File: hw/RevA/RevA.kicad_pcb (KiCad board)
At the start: 4 copper layers, 85 x 54 mm, 94 parts, among them J1 USB_C_Receptacle_USB2.0, J3 DNP Conn_01x02, J4 DNP Conn_02x03_Odd_Even, SW1 SW_Push, SW2 SW_Push, U1 SY8120B1ABC, U2 XC6206P25, U3 SY8120B1ABC, U4 SPI Flash W25Q128JVSIQ, U8 LFE5U-12F-6BG256C, U9 16MHz 20ppm

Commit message: progress
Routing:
- net +3V3: track 112.4 -> 62.4 mm, vias 43 -> 36
- net GND: track 151.4 -> 106.0 mm, vias 94 -> 89
- net /LED_B: track 37.0 -> 0.00 mm, vias 2 -> 0
- net /LED_G: track 35.9 -> 0.00 mm, vias 2 -> 0
- net /LED_R: track 35.0 -> 0.00 mm, vias 2 -> 0
- net /JTAG_TDO: track 57.9 -> 35.2 mm, vias 3 -> 2
- net Net-(U8-PadR1): track 21.9 -> 0.00 mm
- net Net-(U8-PadB11): track 21.7 -> 0.00 mm
- net /FPGA_DONE: track 21.4 -> 0.00 mm
- net Net-(U8-PadB12): track 19.9 -> 0.00 mm
- net Net-(U8-PadA12): track 19.8 -> 0.00 mm
- net Net-(U8-PadT2): track 18.9 -> 0.00 mm
- net /FPGA_~INIT: track 18.6 -> 0.00 mm, vias 2 -> 0
- net Net-(U8-PadA13): track 18.0 -> 0.00 mm
- net Net-(U8-PadC6): track 17.8 -> 0.02 mm, vias 2 -> 0
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
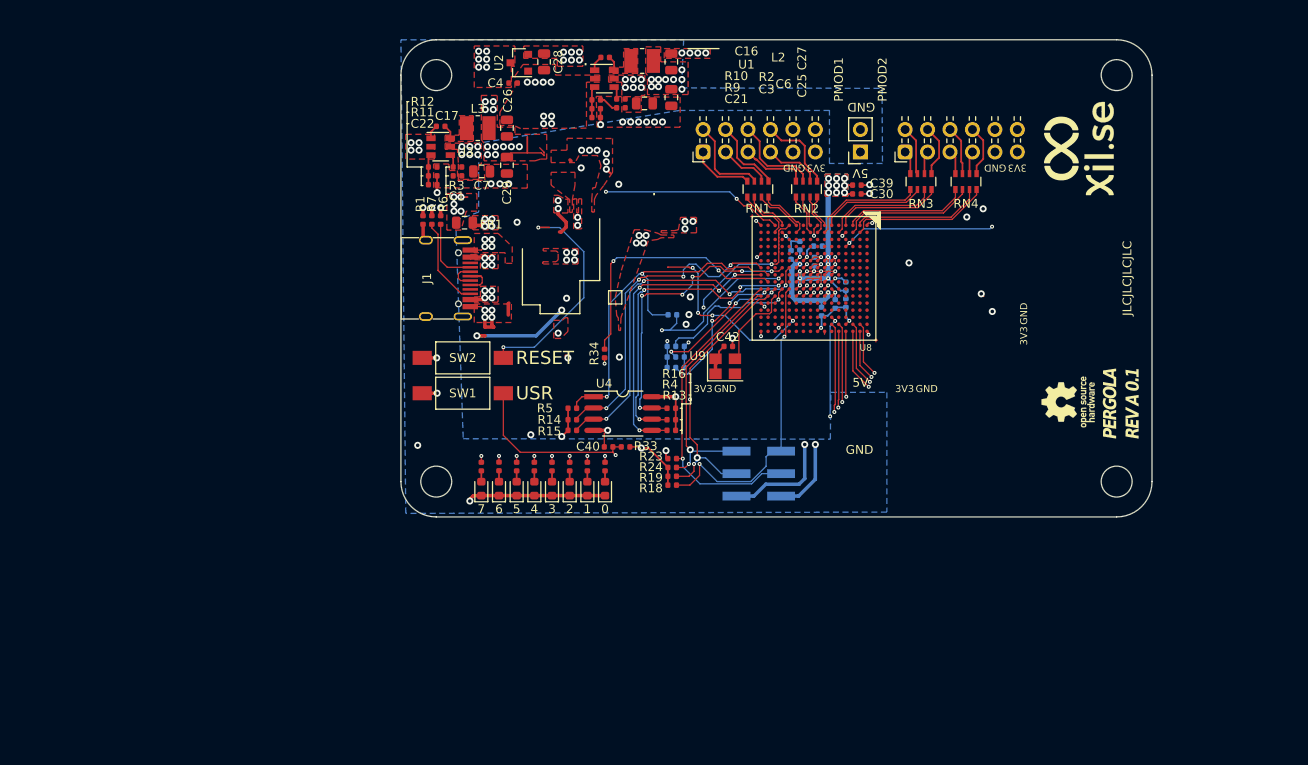
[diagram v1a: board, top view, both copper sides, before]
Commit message: Import pcb shape
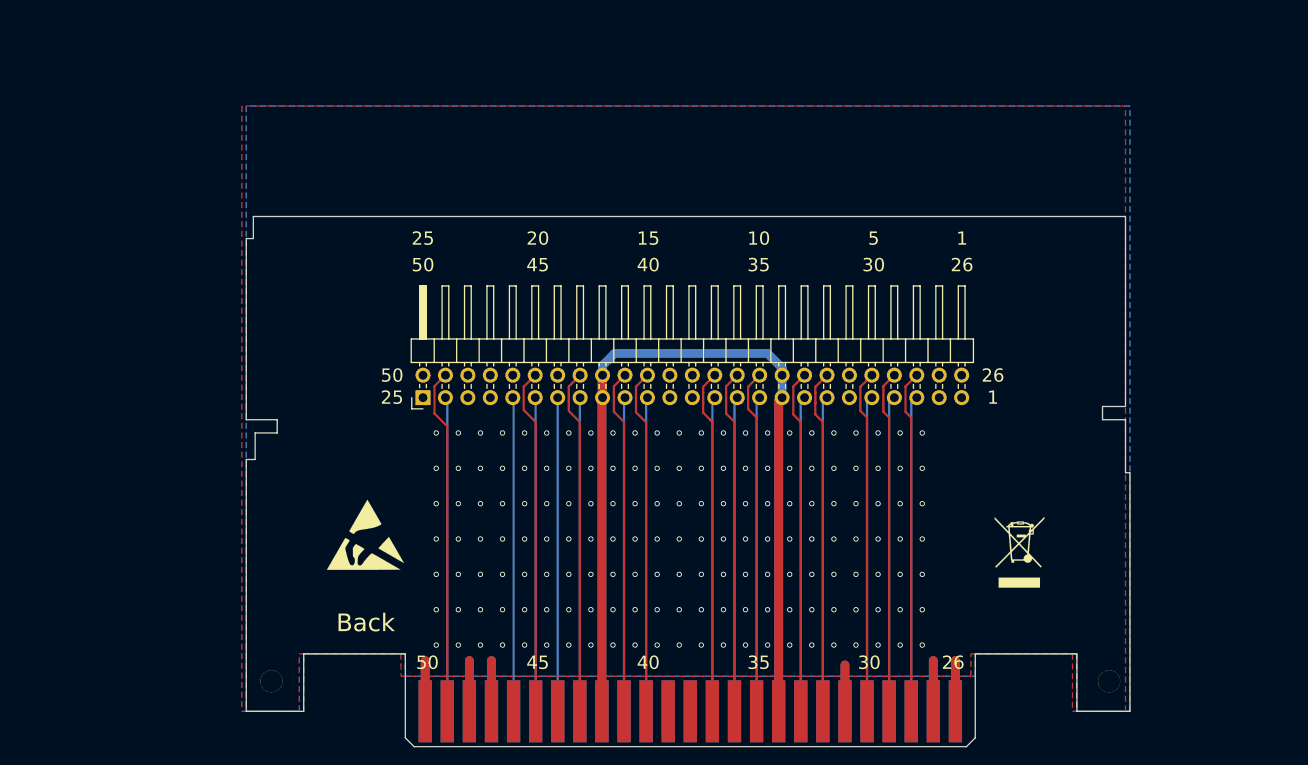
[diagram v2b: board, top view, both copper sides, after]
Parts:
- removed C1, C16, C17, C3, C30, C31, C32, C33, C34, C35, C36, C37, C38, C39, C40, C42: 100n, Capacitor_SMD:C_0402_1005Metric
- removed C21, C22: 22p, Capacitor_SMD:C_0402_1005Metric
- removed C25, C26, C27, C28, C29, C6, C7: 22u, Capacitor_SMD:C_0805_2012Metric
- removed C4: 4u7, Capacitor_SMD:C_0402_1005Metric
- removed D2, D3, D4, D5, D6, D7, D8, D9: LED, LED_SMD:LED_0603_1608Metric
- removed FB1: Ferrite_Bead, Inductor_SMD:L_0805_2012Metric
- removed H1, H2, H3, H4: DNP, MountingHole:MountingHole_3.5mm
- removed J3: DNP Conn_01x02, Connector_PinSocket_2.54mm:PinSocket_1x02_P2.54mm_Vertical
- removed J4: DNP Conn_02x03_Odd_Even, Connector_PinHeader_2.54mm:PinHeader_2x03_P2.54mm_Vertical_SMD
- removed JP7, JP8, JP9: 4K7, ecp5board:JP_3_0402_1005Metric
- removed L2, L3: 4u7 1A, ecp5board:L_1008_1210
- removed LOGO1: Logo_Open_Hardware_Small, Symbol:OSHW-Logo_5.7x6mm_SilkScreen
- removed LOGO2: Logo_Open_Hardware_Small, ecp5board:logo
- removed LOGO3: Logo_Open_Hardware_Small, ecp5board:xil_logo_new
- removed PMOD1, PMOD2: Conn_02x06_Top_Bottom, ecp5board:PMOD_Socket_2x06_P2.54mm_Horizontal
- removed R1: 100K, Resistor_SMD:R_0402_1005Metric
- removed R10: 18K, Resistor_SMD:R_0402_1005Metric
- removed R11, R9: 15K, Resistor_SMD:R_0402_1005Metric
- removed R12: 3K3, Resistor_SMD:R_0402_1005Metric
- removed R13, R14, R15, R16, R2, R25, R26, R27, R28, R29, R3, R30, R31, R32: 10K, Resistor_SMD:R_0402_1005Metric
- removed R18, R19, R23, R24, R33, R34, R5: 4K7, Resistor_SMD:R_0402_1005Metric
- removed R35: DNP, Resistor_SMD:R_0402_1005Metric
- removed R4: 1K, Resistor_SMD:R_0402_1005Metric
- removed R6, R7: 5K1, Resistor_SMD:R_0402_1005Metric
- removed RN1, RN2, RN3, RN4: 22R_x4, Resistor_SMD:R_Array_Convex_4x0603
- removed SW1, SW2: SW_Push, Button_Switch_SMD:SW_SPST_FSMSM
- removed U1, U3: SY8120B1ABC, Package_TO_SOT_SMD:SOT-23-6
- removed U2: XC6206P25, Package_TO_SOT_SMD:SOT-23
- removed U4: SPI Flash W25Q128JVSIQ, ecp5board:SOA008-150-208mil
- removed U8: LFE5U-12F-6BG256C, w_smd_bga:cabga256
- removed U9: 16MHz 20ppm, Crystal:Crystal_SMD_3225-4Pin_3.2x2.5mm
- added CON1: N64-Cartridge, Brutzelkarte:N64-Connector, B.Cu at (132.8, 126.0)
- added REF**: ESD-Logo_8.9x8mm_SilkScreen, Symbol:ESD-Logo_8.9x8mm_SilkScreen, F.Cu at (96.0, 106.0)
- added REF**: WEEE-Logo_5.6x8mm_SilkScreen, Symbol:WEEE-Logo_5.6x8mm_SilkScreen, F.Cu at (170.0, 108.0)
- added REF**: MountingHole_2.5mm_Pad, MountingHole:MountingHole_2.5mm_Pad, F.Cu at (180.2, 122.6)
- added REF**: MountingHole_2.5mm_Pad, MountingHole:MountingHole_2.5mm_Pad, F.Cu at (85.3, 122.6)
- J1: value USB_C_Receptacle_USB2.0 -> Conn_02x25_Odd_Even; footprint Connector_USB_Extra:USB_C_Receptacle_GT-USB-7010 -> Connector_PinHeader_2.54mm:PinHeader_2x25_P2.54mm_Horizontal
- moved J1 13.7 mm to (102.5, 90.5), turned to 90 degrees
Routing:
- net /fpga/N64_VCC: track 0.00 -> 173.5 mm
- net /LED7: track 63.4 -> 0.00 mm, vias 2 -> 0
- net +3V3: track 62.4 -> 0.00 mm, vias 36 -> 0
- net /SW_USER: track 62.0 -> 0.00 mm, vias 3 -> 0
- net /LED6: track 60.0 -> 0.00 mm, vias 2 -> 0
- net /LED5: track 58.5 -> 0.00 mm, vias 2 -> 0
- net /LED4: track 55.1 -> 0.00 mm, vias 2 -> 0
- net /LED3: track 50.4 -> 0.00 mm, vias 2 -> 0
- net /LED2: track 48.8 -> 0.00 mm, vias 2 -> 0
- net /LED1: track 45.3 -> 0.00 mm, vias 2 -> 0
- net /LED0: track 43.6 -> 0.00 mm, vias 2 -> 0
- net /FPGA_SPI_~CS~: track 42.5 -> 0.00 mm, vias 2 -> 0
- net /FPGA_SPI_D2: track 40.9 -> 0.00 mm, vias 4 -> 0
- net /fpga/N64_AD5: track 0.00 -> 39.4 mm
- net /fpga/N64_RAUDIO: track 0.00 -> 39.2 mm
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- added copper zone on B.Cu, net GND
- removed copper zone on B.Cu, net +1V1
- removed copper zone on F.Cu, net +1V1
- removed copper zone on In2.Cu, net +1V1
- removed copper zone on F.Cu, net +2V5
- removed copper zone on In2.Cu, net +2V5
- removed copper zone on F.Cu, net +3V3
- removed copper zone on In2.Cu, net +3V3
- removed copper zone on F.Cu, net /DCDC_OUT
- removed copper zone on In2.Cu, net /DCDC_OUT
- removed copper zone on In1.Cu, net /USB_SHIELD
- removed copper zone on F.Cu, net /VBUS_UNFILTERED
- removed copper zone on In2.Cu, net /VBUS_UNFILTERED
- removed copper zone on In1.Cu, net GND
- removed copper zone on In2.Cu, net GND
- removed copper zone on F.Cu, net Net-(C16-Pad2)
- removed copper zone on F.Cu, net Net-(C17-Pad2)
- removed copper zone on F.Cu, net Net-(L1-Pad2)
- removed copper zone on B.Cu, net VBUS
- removed copper zone on F.Cu, net VBUS
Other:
- board size 85 x 54 mm -> 100 x 60 mm
- copper layers 4 -> 2
- net class Default: clearance 0.127 -> 0.25; trace_width 0.127 -> 0.25; via_dia 0.45 -> 0.6; via_drill 0.2 -> 0.4
- net class differential routing added: clearance 0.4, trace_width 0.25, via_dia 0.6, via_drill 0.4
- rule pad_to_mask_clearance: 0.051 -> 0.13
- rule solder_mask_min_width: 0.25 -> 0.3
- rule trace_clearance: 0.127 -> 0.25
- rule trace_min: 0.0889 -> 0.1
- rule via_min_drill: 0.2 -> 0.3
- rule via_min_size: 0.45 -> 0.5
- board text added: "10"
- board text added: "15"
- board text added: "20"
- board text added: "25"
- board text added: "26"
- board text added: "30"
- board text added: "35"
- board text added: "40"
- board text added: "45"
- board text added: "50"
- board text removed: "."
- board text removed: "0"
- board text removed: "2"
- board text removed: "3"
- board text removed: "3V3"
- board text removed: "4"
- board text removed: "5V"
- board text removed: "6"
- board text removed: "7"
- board text removed: "Designed by @kbeckmann"
- board text removed: "ECP5_CFG_0"
- board text removed: "ECP5_CFG_1"
- board text removed: "ECP5_CFG_2"
- board text removed: "GND"
- board text removed: "IMX_BOOT_MODE_0"
- board text removed: "IMX_BOOT_MODE_1"
- board text removed: "IMX_CFG_0"
- board text removed: "IMX_CFG_1"
- board text removed: "IMX_CFG_2"
- board text removed: "IMX_CFG_3"
- board text removed: "JLCJLCJLCJLC"
- board text removed: "PMOD1"
- board text removed: "PMOD2"
- board text removed: "PMOD3"
- board text removed: "PMOD4"
- board text removed: "PMOD5"
- board text removed: "Place 0R to connect ECP5_MASTER_SPI_CSN to FLASH_CSN"
- board text removed: "RESET"
- board text removed: "SWCLK"
- board text removed: "SWDIO"
- board text removed: "TCK"
- board text removed: "TDI"
- board text removed: "TDO"
- board text removed: "TMS"
- board text removed: "USR"
- board text removed: "VCC"
- board text removed: "https://pergola.xil.se"

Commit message: progress
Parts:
- removed the REF** at (96.0, 106.0)
- removed the REF** at (170.0, 108.0)
- removed the REF** at (180.2, 122.6)
- removed the REF** at (85.3, 122.6)
- added C1: 100n, Capacitor_SMD:C_0402_1005Metric, F.Cu at (73.5, 85.0)
- added C16: 100n, Capacitor_SMD:C_0402_1005Metric, F.Cu at (87.1, 92.1)
- added C17: 100n, Capacitor_SMD:C_0402_1005Metric, F.Cu at (76.4, 82.9)
- added C2: 100n, Capacitor_SMD:C_0402_1005Metric, F.Cu at (87.9, 70.9)
- added C21: 22p, Capacitor_SMD:C_0402_1005Metric, F.Cu at (73.2, 100.7)
- added C22: 22p, Capacitor_SMD:C_0402_1005Metric, F.Cu at (80.3, 93.7)
- added C25: 22u, Capacitor_SMD:C_0805_2012Metric, F.Cu at (62.5, 72.3)
- added C26: 22u, Capacitor_SMD:C_0805_2012Metric, F.Cu at (67.0, 72.2)
- added C27: 22u, Capacitor_SMD:C_0805_2012Metric, F.Cu at (68.3, 91.1)
- added C28: 22u, Capacitor_SMD:C_0805_2012Metric, F.Cu at (75.5, 71.9)
- added C29: 22u, Capacitor_SMD:C_0805_2012Metric, F.Cu at (64.0, 83.6)
- added C3: 100n, Capacitor_SMD:C_0402_1005Metric, F.Cu at (87.9, 68.9)
- added C30: 100n, Capacitor_SMD:C_0402_1005Metric, F.Cu at (82.8, 75.7)
- added C31: 100n, Capacitor_SMD:C_0402_1005Metric, F.Cu at (76.0, 81.0)
- added C32: 100n, Capacitor_SMD:C_0402_1005Metric, F.Cu at (87.1, 90.1)
- added C33: 100n, Capacitor_SMD:C_0402_1005Metric, F.Cu at (77.4, 94.8)
- added C34: 100n, Capacitor_SMD:C_0402_1005Metric, F.Cu at (85.0, 72.1)
- added C35: 100n, Capacitor_SMD:C_0402_1005Metric, F.Cu at (79.9, 77.7)
- added C36: 100n, Capacitor_SMD:C_0402_1005Metric, F.Cu at (73.2, 98.7)
- added C37: 100n, Capacitor_SMD:C_0402_1005Metric, F.Cu at (79.9, 75.7)
- added C38: 100n, Capacitor_SMD:C_0402_1005Metric, F.Cu at (73.5, 83.0)
- added C39: 100n, Capacitor_SMD:C_0402_1005Metric, F.Cu at (81.5, 89.8)
- added C4: 4u7, Capacitor_SMD:C_0402_1005Metric, F.Cu at (80.3, 91.8)
- added C40: 100n, Capacitor_SMD:C_0402_1005Metric, F.Cu at (70.3, 100.7)
- added C42: 100n, Capacitor_SMD:C_0402_1005Metric, F.Cu at (74.5, 96.8)
- added C5: 100n, Capacitor_SMD:C_0402_1005Metric, F.Cu at (78.9, 81.0)
- added C6: 22u, Capacitor_SMD:C_0805_2012Metric, F.Cu at (79.7, 67.3)
- added C7: 22u, Capacitor_SMD:C_0805_2012Metric, F.Cu at (58.1, 72.3)
- added D2: LED, LED_SMD:LED_0603_1608Metric, F.Cu at (75.0, 74.7)
- added D3: LED, LED_SMD:LED_0603_1608Metric, F.Cu at (84.3, 65.8)
- added D4: LED, LED_SMD:LED_0603_1608Metric, F.Cu at (68.1, 96.5)
- added D5: LED, LED_SMD:LED_0603_1608Metric, F.Cu at (64.0, 100.6)
- added D6: LED, LED_SMD:LED_0603_1608Metric, F.Cu at (84.3, 63.2)
- added D7: LED, LED_SMD:LED_0603_1608Metric, F.Cu at (64.0, 98.0)
- added D8: LED, LED_SMD:LED_0603_1608Metric, F.Cu at (68.1, 93.9)
- added D9: LED, LED_SMD:LED_0603_1608Metric, F.Cu at (60.0, 60.9)
- added DBG1: Conn_02x06_Top_Bottom, ecp5board:PMOD_Socket_2x06_P2.54mm_Horizontal, F.Cu at (125.9, 60.2)
- added FB1: Ferrite_Bead, Inductor_SMD:L_0805_2012Metric, F.Cu at (70.1, 60.4)
- added J2: Micro_SD_Card, Connector_Card:microSD_HC_Molex_104031-0811, F.Cu at (191.5, 67.0)
- added J3: DNP Conn_01x02, Connector_PinSocket_2.54mm:PinSocket_1x02_P2.54mm_Vertical, F.Cu at (160.2, 66.2)
- added JP1: 4K7, Connector_PinHeader_2.54mm:PinHeader_1x03_P2.54mm_Horizontal, F.Cu at (106.0, 92.5)
- added JP7: 4K7, ecp5board:JP_3_0402_1005Metric, F.Cu at (74.8, 88.8)
- added JP8: 4K7, ecp5board:JP_3_0402_1005Metric, F.Cu at (65.5, 81.0)
- added JP9: 4K7, ecp5board:JP_3_0402_1005Metric, F.Cu at (73.9, 60.0)
- added L2: 4u7 1A, ecp5board:L_1008_1210, F.Cu at (76.4, 108.6)
- added L3: 4u7 1A, ecp5board:L_1008_1210, F.Cu at (82.0, 108.6)
- added LOGO1: Logo_Open_Hardware_Small, Symbol:OSHW-Logo_5.7x6mm_SilkScreen, F.Cu at (189.8, 105.5)
- added LOGO3: Logo_Open_Hardware_Small, ecp5board:xil_logo_new, F.Cu at (112.0, 105.5)
- added PMOD1: Conn_02x06_Top_Bottom, ecp5board:PMOD_Socket_2x06_P2.54mm_Horizontal, F.Cu at (148.7, 60.2)
- added PMOD2: Conn_02x06_Top_Bottom, ecp5board:PMOD_Socket_2x06_P2.54mm_Horizontal, F.Cu at (171.6, 60.2)
- added R1: 100K, Resistor_SMD:R_0402_1005Metric, F.Cu at (77.4, 92.8)
- added R10: 18K, Resistor_SMD:R_0402_1005Metric, F.Cu at (88.0, 84.2)
- added R11: 15K, Resistor_SMD:R_0402_1005Metric, F.Cu at (72.0, 90.8)
- added R12: 3K3, Resistor_SMD:R_0402_1005Metric, F.Cu at (74.9, 90.8)
- added R13: 10K, Resistor_SMD:R_0402_1005Metric, F.Cu at (74.1, 77.0)
- added R14: 10K, Resistor_SMD:R_0402_1005Metric, F.Cu at (67.5, 98.7)
- added R15: 10K, Resistor_SMD:R_0402_1005Metric, F.Cu at (77.0, 79.0)
- added R16: 10K, Resistor_SMD:R_0402_1005Metric, F.Cu at (88.0, 80.2)
- added R17: 22R, Resistor_SMD:R_0402_1005Metric, F.Cu at (88.0, 86.2)
- added R18: 4K7, Resistor_SMD:R_0402_1005Metric, F.Cu at (79.2, 73.7)
- added R19: 4K7, Resistor_SMD:R_0402_1005Metric, F.Cu at (87.8, 64.9)
- added R2: 10K, Resistor_SMD:R_0402_1005Metric, F.Cu at (87.9, 66.9)
- added R20: 1K, Resistor_SMD:R_0402_1005Metric, F.Cu at (71.6, 95.5)
- added R21: 4K7, Resistor_SMD:R_0402_1005Metric, F.Cu at (67.7, 85.0)
- added R22: 10K, Resistor_SMD:R_0402_1005Metric, F.Cu at (73.2, 81.0)
- added R23: 4K7, Resistor_SMD:R_0402_1005Metric, F.Cu at (67.5, 100.7)
- added R24: 4K7, Resistor_SMD:R_0402_1005Metric, F.Cu at (77.0, 77.0)
- added R25: 10K, Resistor_SMD:R_0402_1005Metric, F.Cu at (82.1, 71.8)
- added R26: 10K, Resistor_SMD:R_0402_1005Metric, F.Cu at (70.6, 83.0)
- added R27: 10K, Resistor_SMD:R_0402_1005Metric, F.Cu at (85.0, 68.1)
- added R28: 10K, Resistor_SMD:R_0402_1005Metric, F.Cu at (78.6, 89.8)
- added R29: 10K, Resistor_SMD:R_0402_1005Metric, F.Cu at (70.4, 98.7)
- added R3: 10K, Resistor_SMD:R_0402_1005Metric, F.Cu at (88.0, 82.2)
- added R30: 10K, Resistor_SMD:R_0402_1005Metric, F.Cu at (74.1, 79.0)
- added R31: 10K, Resistor_SMD:R_0402_1005Metric, F.Cu at (88.0, 78.2)
- added R32: 10K, Resistor_SMD:R_0402_1005Metric, F.Cu at (74.5, 92.8)
- added R33: 4K7, Resistor_SMD:R_0402_1005Metric, F.Cu at (74.5, 94.8)
- added R34: 4K7, Resistor_SMD:R_0402_1005Metric, F.Cu at (85.0, 70.1)
- added R35: 10K, Resistor_SMD:R_0402_1005Metric, F.Cu at (70.6, 85.0)
- added R36: 10K, Resistor_SMD:R_0402_1005Metric, F.Cu at (82.1, 73.7)
- added R37: 10K, Resistor_SMD:R_0402_1005Metric, F.Cu at (87.0, 88.2)
- added R4: 1K, Resistor_SMD:R_0402_1005Metric, F.Cu at (79.2, 69.8)
- added R5: 4K7, Resistor_SMD:R_0402_1005Metric, F.Cu at (67.7, 83.0)
- added R6: 5K1, Resistor_SMD:R_0402_1005Metric, F.Cu at (71.6, 93.6)
- added R7: 5K1, Resistor_SMD:R_0402_1005Metric, F.Cu at (87.8, 63.0)
- added R8: 22R, Resistor_SMD:R_0402_1005Metric, F.Cu at (82.1, 69.8)
- added R9: 15K, Resistor_SMD:R_0402_1005Metric, F.Cu at (79.2, 71.8)
- added REF**: MountingHole_2.5mm_Pad, MountingHole:MountingHole_2.5mm_Pad, F.Cu at (197.7, 112.6)
- added REF**: MountingHole_2.5mm_Pad, MountingHole:MountingHole_2.5mm_Pad, F.Cu at (102.8, 112.6)
- added RN1: 22R_x4, Resistor_SMD:R_Array_Convex_4x0603, F.Cu at (144.0, 77.0)
- added RN10: 22R_x4, Resistor_SMD:R_Array_Convex_4x0603, F.Cu at (149.5, 106.0)
- added RN11: 22R_x4, Resistor_SMD:R_Array_Convex_4x0603, F.Cu at (140.5, 106.0)
- added RN12: 22R_x4, Resistor_SMD:R_Array_Convex_4x0603, F.Cu at (131.5, 106.0)
- added RN2: 22R_x4, Resistor_SMD:R_Array_Convex_4x0603, F.Cu at (149.5, 77.0)
- added RN3: 22R_x4, Resistor_SMD:R_Array_Convex_4x0603, F.Cu at (167.0, 77.0)
- added RN4: 22R_x4, Resistor_SMD:R_Array_Convex_4x0603, F.Cu at (172.5, 77.0)
- added RN5: 22R_x4, Resistor_SMD:R_Array_Convex_4x0603, F.Cu at (158.5, 106.0)
- added RN6: 22R_x4, Resistor_SMD:R_Array_Convex_4x0603, F.Cu at (154.0, 106.0)
- added RN7: 22R_x4, Resistor_SMD:R_Array_Convex_4x0603, F.Cu at (145.0, 106.0)
- added RN8: 22R_x4, Resistor_SMD:R_Array_Convex_4x0603, F.Cu at (136.0, 106.0)
- added RN9: 22R_x4, Resistor_SMD:R_Array_Convex_4x0603, F.Cu at (163.0, 106.0)
- added SW1: SW_Push, Button_Switch_SMD:SW_SPST_FSMSM, F.Cu at (192.0, 77.0)
- added U1: SY8120B1ABC, Package_TO_SOT_SMD:SOT-23-6, F.Cu at (75.7, 63.3)
- added U2: XC6206P25, Package_TO_SOT_SMD:SOT-23, F.Cu at (70.4, 77.8)
- added U3: SY8120B1ABC, Package_TO_SOT_SMD:SOT-23-6, F.Cu at (80.8, 101.2)
- added U4: SPI Flash W25Q128JVSIQ, ecp5board:SOA008-150-208mil, F.Cu at (129.2, 86.2)
- added U6: IS42S16320F-7TL, Package_SO:TSOP-II-54_22.2x10.16mm_P0.8mm, F.Cu at (176.5, 90.0)
- added U7: SPI Flash W25Q128JVSIQ, ecp5board:SOA008-150-208mil, F.Cu at (129.5, 93.2)
- added U8: LFE5U-12F-6BG256C, w_smd_bga:cabga256, F.Cu at (150.0, 90.0)
- added U9: 16MHz 20ppm, Crystal:Crystal_SMD_3225-4Pin_3.2x2.5mm, F.Cu at (160.0, 77.0)
- CON1: footprint Brutzelkarte:N64-Connector -> ecp5board:N64-Connector
- J1: value Conn_02x25_Odd_Even -> USB_C_Receptacle_USB2.0; footprint Connector_PinHeader_2.54mm:PinHeader_2x25_P2.54mm_Horizontal -> Connector_USB_Extra:USB_C_Receptacle_GT-USB-7010
- moved J1 23.2 mm to (105.2, 67.5), turned to 270 degrees
- moved CON1 20.2 mm to (150.2, 116.0)
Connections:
- CON1 pad 10: /fpga/N64_READ -> /N64_READ
- CON1 pad 11: /fpga/N64_AD11 -> /N64_AD11
- CON1 pad 12: /fpga/N64_AD10 -> /N64_AD10
- CON1 pad 15: /fpga/N64_AD9 -> /N64_AD9
- CON1 pad 16: /fpga/N64_AD8 -> /N64_AD8
- CON1 pad 17: /fpga/N64_VCC -> /N64_VCC
- CON1 pad 18: /fpga/N64_CIC_DIO -> /N64_CIC_DIO
- CON1 pad 19: /fpga/N64_SI_CLK -> /N64_SI_CLK
- CON1 pad 20: /fpga/N64_CR -> /N64_CR
- CON1 pad 21: /fpga/N64_EEP_SDAT -> /N64_EEP_SDAT
- CON1 pad 24: /fpga/N64_LAUDIO -> /N64_LAUDIO
- CON1 pad 28: /fpga/N64_AD0 -> /N64_AD0
- CON1 pad 29: /fpga/N64_AD1 -> /N64_AD1
- CON1 pad 3: /fpga/N64_AD15 -> /N64_AD15
- CON1 pad 30: /fpga/N64_AD2 -> /N64_AD2
- CON1 pad 32: /fpga/N64_AD3 -> /N64_AD3
- CON1 pad 33: /fpga/N64_ALEL -> /N64_ALEL
- CON1 pad 34: /fpga/N64_VCC -> /N64_VCC
- CON1 pad 35: /fpga/N64_ALEH -> /N64_ALEH
- CON1 pad 36: /fpga/N64_AD4 -> /N64_AD4
- CON1 pad 37: /fpga/N64_AD5 -> /N64_AD5
- CON1 pad 4: /fpga/N64_AD14 -> /N64_AD14
- CON1 pad 40: /fpga/N64_AD6 -> /N64_AD6
- CON1 pad 41: /fpga/N64_AD7 -> /N64_AD7
- CON1 pad 42: /fpga/N64_VCC -> /N64_VCC
- CON1 pad 43: /fpga/N64_CIC_DCLK -> /N64_CIC_DCLK
- CON1 pad 45: /fpga/N64_NMI -> /N64_NMI
- CON1 pad 49: /fpga/N64_RAUDIO -> /N64_RAUDIO
- CON1 pad 5: /fpga/N64_AD13 -> /N64_AD13
- CON1 pad 7: /fpga/N64_AD12 -> /N64_AD12
- CON1 pad 8: /fpga/N64_WRITE -> /N64_WRITE
- CON1 pad 9: /fpga/N64_VCC -> /N64_VCC
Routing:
- net /fpga/N64_VCC: track 173.5 -> 0.00 mm
- net /fpga/N64_AD5: track 39.4 -> 0.00 mm
- net /fpga/N64_RAUDIO: track 39.2 -> 0.00 mm
- net /fpga/N64_NMI: track 39.1 -> 0.00 mm
- net /fpga/N64_CIC_DCLK: track 39.1 -> 0.00 mm
- net /fpga/N64_AD6: track 39.1 -> 0.00 mm
- net /fpga/N64_AD7: track 39.0 -> 0.00 mm
- net /fpga/N64_ALEH: track 39.0 -> 0.00 mm
- net /fpga/N64_AD4: track 39.0 -> 0.00 mm
- net /fpga/N64_AD3: track 38.9 -> 0.00 mm
- net /fpga/N64_ALEL: track 38.9 -> 0.00 mm
- net /fpga/N64_AD2: track 38.9 -> 0.00 mm
- net /fpga/N64_AD0: track 38.8 -> 0.00 mm
- net /fpga/N64_AD1: track 38.8 -> 0.00 mm
- net /fpga/N64_AD14: track 35.8 -> 0.00 mm
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
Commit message: progress
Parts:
- removed C4: 4u7, Capacitor_SMD:C_0402_1005Metric
- removed RN12: 22R_x4, Resistor_SMD:R_Array_Convex_4x0603
- added D1: 1N914, Diode_SMD:D_SOD-323_HandSoldering, F.Cu at (113.6, 72.2)
- added R38: 1K1, Resistor_SMD:R_0402_1005Metric, F.Cu at (113.6, 69.4)
- moved LOGO1 107.9 mm to (82.5, 117.5)
- moved C7 60.5 mm to (113.8, 96.0), turned to 90 degrees
- moved R23 60.1 mm to (122.2, 76.0), turned to 90 degrees
- moved C25 60.0 mm to (116.0, 99.5), turned to 270 degrees
- moved C26 53.6 mm to (116.0, 93.8), turned to 90 degrees
- moved C29 52.4 mm to (116.0, 90.3), turned to 270 degrees
- moved R6 51.9 mm to (113.8, 63.4), turned to 270 degrees
- moved U1 51.5 mm to (108.0, 103.5)
- moved C6 51.0 mm to (113.8, 105.2), turned to 90 degrees
- moved C27 49.2 mm to (116.0, 103.1), turned to 90 degrees
- moved FB1 46.6 mm to (109.5, 85.2), turned to 180 degrees
- moved R1 45.7 mm to (112.4, 63.4), turned to 270 degrees
- moved R9 45.7 mm to (107.0, 108.0)
- moved LOGO3 45.5 mm to (68.0, 117.0)
- moved R18 45.4 mm to (124.6, 76.0), turned to 270 degrees
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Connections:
- CON1 pad 13: Net-(CON1-Pad13) -> +12V
- CON1 pad 39: Net-(CON1-Pad39) -> +12V
- DBG1 pad 10: GND -> /DEBUG_2
- DBG1 pad 9: GND -> /DEBUG_1
- FB1 pad 1: VBUS -> Net-(FB1-Pad1)
- FB1 pad 2: Net-(FB1-Pad2) -> /V_SUPPLY
- J1 pad A4: Net-(FB1-Pad2) -> VBUS
- J1 pad A9: Net-(FB1-Pad2) -> VBUS
- J1 pad B4: Net-(FB1-Pad2) -> VBUS
- J1 pad B9: Net-(FB1-Pad2) -> VBUS
- JP1 pad 1: +12V -> VBUS
- JP1 pad 2: /V_SUPPLY -> Net-(FB1-Pad1)
- JP1 pad 3: VBUS -> +12V
- RN8 pad 4: Net-(RN8-Pad4) -> /N64_RAUDIO
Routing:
- net +12V: track 0.00 -> 93.0 mm, vias 0 -> 2
- net GND: track 68.0 -> 110.4 mm, vias 0 -> 52
- net +3V3: track 0.00 -> 25.7 mm, vias 0 -> 15
- net /USB_SHIELD: track 0.00 -> 23.6 mm
- net +1V1: track 0.00 -> 22.8 mm, vias 0 -> 10
- net Net-(J1-PadB5): track 0.00 -> 22.0 mm
- net VBUS: track 0.00 -> 18.6 mm, vias 0 -> 8
- net Net-(J1-PadA5): track 0.00 -> 15.6 mm
- net Net-(FB1-Pad1): track 0.00 -> 13.6 mm
- net Net-(J1-PadA6): track 0.00 -> 10.2 mm
- net Net-(J1-PadA7): track 0.00 -> 7.89 mm
- net /V_SUPPLY: track 0.00 -> 6.96 mm, vias 0 -> 10
- net +2V5: track 0.00 -> 4.28 mm, vias 0 -> 5
- net /USB_DP: track 0.00 -> 3.79 mm
- net Net-(C21-Pad1): track 0.00 -> 3.74 mm
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- added copper zone on F.Cu, net +1V1
- added copper zone on F.Cu, net +2V5
- added copper zone on F.Cu, net +3V3
- added copper zone on In2.Cu, net +3V3
- added copper zone on F.Cu, net /V_SUPPLY
- added copper zone on In2.Cu, net /V_SUPPLY
- added copper zone on In1.Cu, net GND
- added copper zone on In2.Cu, net GND
- added copper zone on F.Cu, net Net-(C16-Pad2)
- added copper zone on F.Cu, net Net-(C17-Pad2)
- added copper zone on F.Cu, net VBUS
- added copper zone on In1.Cu, net VBUS
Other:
- copper layers 2 -> 4
- net class Default: clearance 0.25 -> 0.127; trace_width 0.25 -> 0.127; via_dia 0.6 -> 0.45; via_drill 0.4 -> 0.2
- net class differential routing removed
- rule trace_clearance: 0.25 -> 0.127
- rule trace_min: 0.1 -> 0.0889
- rule via_min_drill: 0.3 -> 0.2
- rule via_min_size: 0.5 -> 0.45
- board text added: "N64 12V"
- board text added: "USB 5V"
